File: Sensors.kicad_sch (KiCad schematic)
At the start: 32 parts, among them U13 BME280, U16 BNO085, U19 BME280, U7 BNO085

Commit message: stuff
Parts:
- removed D?: 1N4148, digikey-footprints:Diode_DO-35_P10mm, symbol dk_Diodes-Rectifiers-Single:1N4148
- removed R?: 27k, symbol Device:R
- removed R? (x2): 1k, symbol Device:R
- removed R?: 240, symbol Device:R
- added D18: D, symbol Device:D
- added R23, R25: 1k, symbol Device:R
- added R24: 240, symbol Device:R
- added R26: 27k, symbol Device:R
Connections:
- net 3.3v: now also R26.1
- net GND: now also D18.1 (K), R23.2
- net Probe: now also R25.1
- net Signal: now also R23.1, R24.1
- net at Q?.1 (G): now also R25.2, R26.2
- new net: D18.2 (A), R24.2

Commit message: stuff
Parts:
- gave numbers to parts that had none: 5
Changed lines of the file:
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@@
 	)
 	(no_connect
-		(at 31.75 99.06)
+		(at 217.17 40.64)
 	)
 	(no_connect
-		(at 95.25 40.64)
+		(at 31.75 99.06)
 	)
 	(no_connect
-		(at 156.21 66.04)
+		(at 95.25 40.64)
 	)
 	(no_connect
@@
 		(dnp no)
 		(fields_autoplaced yes)
-		(property "Reference" "J?"
+		(property "Reference" "J18"
 			(at 99.06 166.3699 0)
 			(effects
@@
 			(project "CM4IOv5"
 				(path "/e63e39d7-6ac0-4ffd-8aa3-1841a4541b55/d818c5c4-22e1-4750-8cc8-fe8a67dac1ec"
-					(reference "J?")
+					(reference "J18")
 					(unit 1)
 				)
@@
 		(dnp no)
 		(fields_autoplaced yes)
-		(property "Reference" "J?"
+		(property "Reference" "J17"
 			(at 99.06 152.3999 0)
 			(effects
@@
 			(project "CM4IOv5"
 				(path "/e63e39d7-6ac0-4ffd-8aa3-1841a4541b55/d818c5c4-22e1-4750-8cc8-fe8a67dac1ec"
-					(reference "J?")
+					(reference "J17")
 					(unit 1)
 				)
@@
 		(dnp no)
 		(fields_autoplaced yes)
-		(property "Reference" "J?"
+		(property "Reference" "J19"
 			(at 99.06 180.3399 0)
 			(effects
@@
 			(project "CM4IOv5"
 				(path "/e63e39d7-6ac0-4ffd-8aa3-1841a4541b55/d818c5c4-22e1-4750-8cc8-fe8a67dac1ec"
-					(reference "J?")
+					(reference "J19")
 					(unit 1)
 				)
@@
 		(dnp no)
 		(fields_autoplaced yes)
-		(property "Reference" "J?"
+		(property "Reference" "J16"
 			(at 99.06 138.4299 0)
 			(effects
@@
 			(project "CM4IOv5"
 				(path "/e63e39d7-6ac0-4ffd-8aa3-1841a4541b55/d818c5c4-22e1-4750-8cc8-fe8a67dac1ec"
-					(reference "J?")
+					(reference "J16")
 					(unit 1)
 				)
@@
 		(dnp no)
 		(fields_autoplaced yes)
-		(property "Reference" "Q?"
+		(property "Reference" "Q1"
 			(at 53.34 147.3199 0)
 			(effects
@@
 			(project "CM4IOv5"
 				(path "/e63e39d7-6ac0-4ffd-8aa3-1841a4541b55/d818c5c4-22e1-4750-8cc8-fe8a67dac1ec"
-					(reference "Q?")
+					(reference "Q1")
 					(unit 1)
 				)

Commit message: stuff
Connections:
- net 3.3v renamed +3.3V

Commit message: minor erc fixes
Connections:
- no-connect marks 6 -> 7
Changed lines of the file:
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@@
+	)
+	(no_connect
+		(at 34.29 66.04)
 	)
 	(no_connect

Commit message: stuff
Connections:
- no-connect marks 7 -> 8
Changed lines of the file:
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@@
+	)
+	(no_connect
+		(at 156.21 66.04)
 	)
 	(no_connect

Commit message: stuff
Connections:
- no-connect marks 8 -> 6
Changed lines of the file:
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@@
-	)
-	(no_connect
-		(at 34.29 66.04)
 	)
 	(no_connect
@@
 	)
 	(no_connect
-		(at 156.21 66.04)
-	)
-	(no_connect

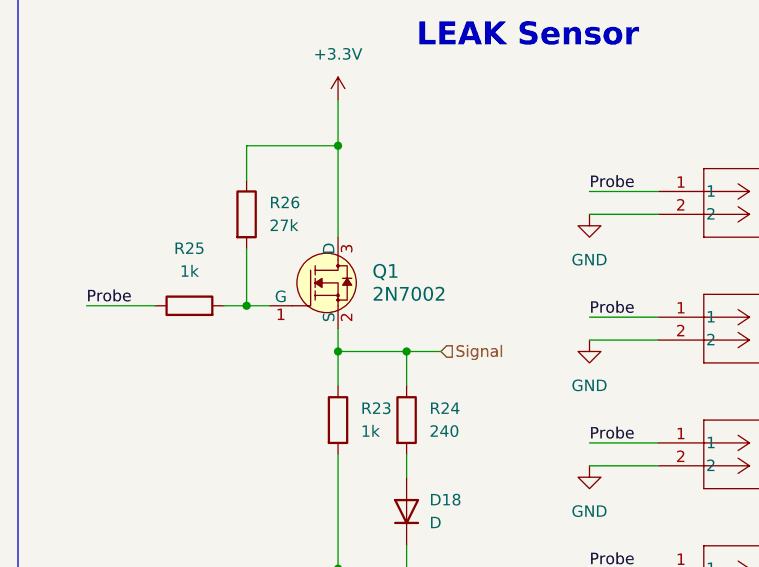
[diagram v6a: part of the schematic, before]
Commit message: assigned footprints
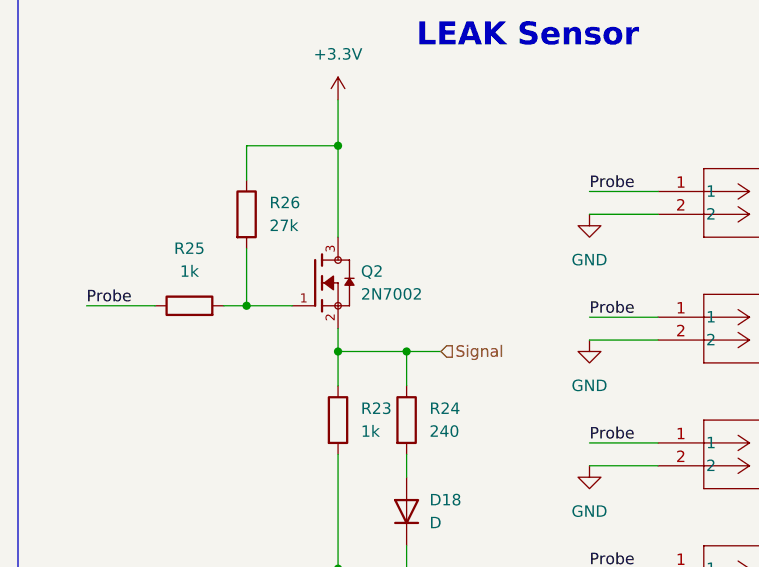
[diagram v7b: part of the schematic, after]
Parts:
- removed Q1: 2N7002, digikey-footprints:SOT-23-3, symbol dk_Transistors-FETs-MOSFETs-Single:2N7002
- added Q2: 2N7002, 2N7002:TRANS_2N7002, symbol 2N7002:2N7002
- C13, C14, C15, C16, C17, C18: footprint (none) -> Capacitor_SMD:C_0805_2012Metric
- D18: footprint (none) -> LED_SMD:LED_0805_2012Metric
- J16, J17, J18, J19: footprint CONN_SM02B-GHS_JST -> SM02B_GHS_TB:CONN_SM02B-GHS_JST
- JP10, JP7, JP8, JP9: footprint (none) -> Jumper:SolderJumper-3_P1.3mm_Open_RoundedPad1.0x1.5mm
- R20, R23, R24, R25, R26, R27, R28, R31, R32, R36, R47, R48: footprint (none) -> Resistor_SMD:R_0805_2012Metric
- U16, U7: footprint BNO085:IC_BNO085 -> BNO085:SQFN36_M2_MCH
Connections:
- net +3.3V: now also Q2.3
- net Signal: now also Q2.2
- net at R25.2, R26.2: now also Q2.1

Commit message: stuff
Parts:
- removed U13, U19: BME280, digikey-footprints:Pressure_Sensor_LGA-8_2.5x2.5mm_BME280, symbol dk_Humidity-Moisture-Sensors:BME280
- added U15, U17: BME280, BME280:DFN8_0p65_2p5SQ_BOS, symbol BME280:BME280
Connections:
- net +3.3V: now also U15.2 (CSB), U15.6 (VDDIO), U15.8 (VDD), U17.2 (CSB), U17.6 (VDDIO), U17.8 (VDD)
- net ENV_SCL: now also U17.4 (SCK)
- net ENV_SCL1: now also U15.4 (SCK)
- net ENV_SDA: now also U17.3 (SDI)
- net ENV_SDA1: now also U15.3 (SDI)
- net GND: now also U15.1 (GND), U15.7 (GND), U17.1 (GND), U17.7 (GND)
